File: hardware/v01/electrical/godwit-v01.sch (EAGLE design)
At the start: 23 parts, among them J1 USB-MINIB-M26FTR, U1 BQ24251, U2 LM3668-3034

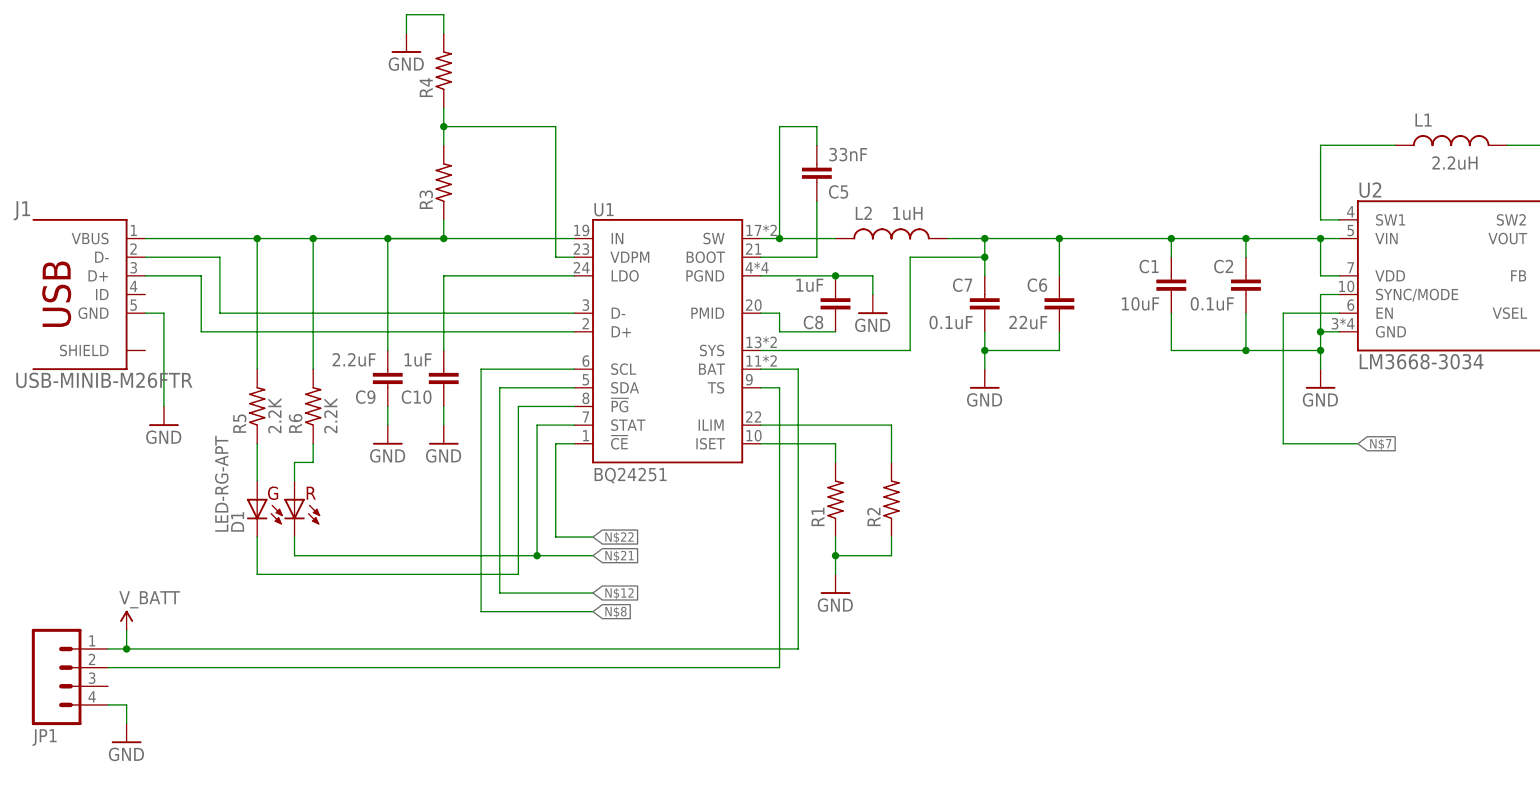
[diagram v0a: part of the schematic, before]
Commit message: rearranged and added circuits
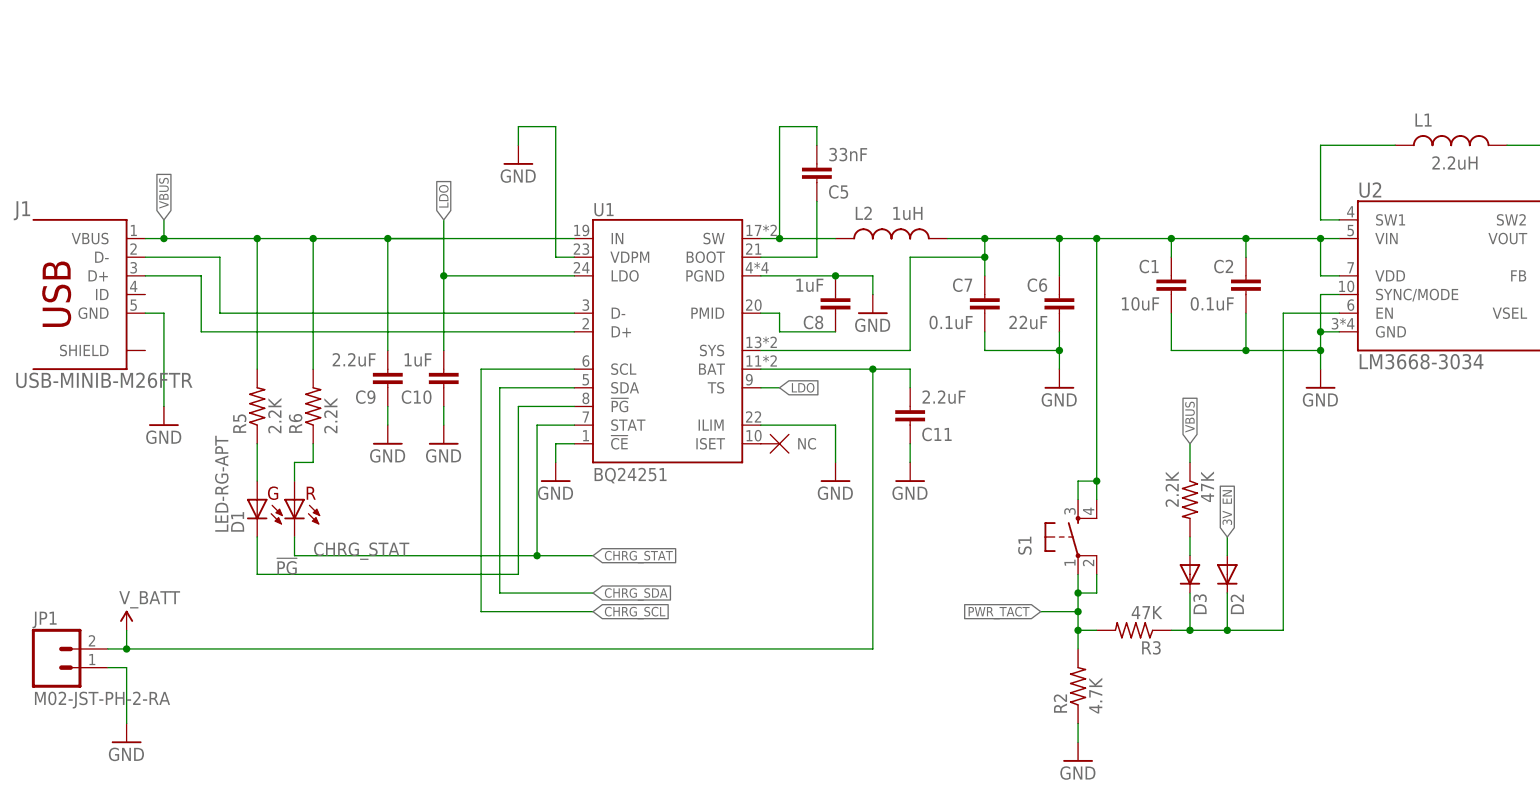
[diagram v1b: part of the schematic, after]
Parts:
- removed R1, R4: (no value), hybridpi-rcl:R-US_R0603
- added 47K: 2.2K, hybridpi-rcl:R-US_R0603
- added C11: 2.2uF, hybridpi-rcl:C-EUC0603
- added D2, D3: (no value), hybridpi-discrete-semi:DIODESOD523
- added S1: (no value), hybridpi-electromechanical:TAC_SWITCHPTH
- added U$1: NC, hybridpi-aesthetics:NC
- C10, C8: VOLTAGE (none) -> >=10V
- C5: VOLTAGE (none) -> >15
- JP1: value (none) -> M02-JST-PH-2-RA; device hybridpi-connector:M04-JST-PH-4-RA -> hybridpi-connector:M02-JST-PH-2-RA
- R2: value (none) -> 4.7K
- R3: value (none) -> 47K
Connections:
- net N$12 renamed CHRG_SDA
- net N$20 renamed !PG!
- net N$21 renamed CHRG_STAT
- net N$8 renamed CHRG_SCL
- removed net N$10: R2.2, U1.ILIM
- removed net N$11: R3.2, R4.1, U1.VDPM
- removed net N$13: JP1.2, U1.TS
- removed net N$14: C10.2, U1.LDO
- removed net N$19: C9.2, J1.VBUS, R3.1, R5.2, R6.2, U1.IN
- removed net N$22: U1.!CE!
- new net 3V_EN: D2.A
- new net LDO: C10.2, U1.LDO, U1.TS
- new net N$8: 47K.2, D3.A
- new net PWR_TACT: R2.2, R3.2, S1.1, S1.2
- new net VBUS: 47K.1, C9.2, J1.VBUS, R5.2, R6.2, U1.IN
- net GND: now also C11.1, JP1.1, U1.!CE!, U1.ILIM, U1.VDPM; no longer JP1.4, R1.1, R4.2
- net N$4: now also S1.3, S1.4
- net N$7: now also U$1.NC, U1.ISET; no longer U2.EN
- net N$9: now also D2.C, D3.C, R3.1, U2.EN; no longer R1.2, U1.ISET
- net V_BATT: now also C11.2, JP1.2; no longer JP1.1
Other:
- moved on the sheet: R2, R3

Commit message: Added sensing circuitry.
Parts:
- added C12, C16: 1uF, hybridpi-rcl:C-EUC0603
- added C13: 4.7uF, hybridpi-rcl:C-EUC0603
- added C14, C15, C17, C18: 0.1uF, hybridpi-rcl:C-EUC0603
- added R4, R7, R8: 220, hybridpi-rcl:R-US_R0603
- added R9: 470K, hybridpi-rcl:R-US_R0603
- added U$10, U$11, U$12, U$2, U$3, U$4, U$5, U$6, U$7, U$8, U$9: NC, hybridpi-aesthetics:NC
- added U3: UC530, hybridpi-rf:UC530
- added U4: AAT4280A, hybridpi-poweric:AAT4280A
- added U5: BMP180, hybridpi-sensor:BMP180
- added U6: MAG3110, hybridpi-sensor:MAG3110
- R1: value 2.2K -> 47K
- R2: value 4.7K -> 2.2K
- renumbered 47K to R1
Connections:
- net N$16 renamed USB_D-
- net N$17 renamed USB_D+
- new net BAR_SCL: U5.SCL
- new net BAR_SDA: U5.SDA
- new net GPS_RX: R7.2
- new net GPS_TX: R4.2
- new net MAG_SCL: U6.SCL
- new net MAG_SDA: U6.SDA
- new net N$10: U$2.NC, U3.TX1
- new net N$11: U$3.NC, U3.RX1
- new net N$12: U$4.NC, U3.PPS
- new net N$13: U$5.NC, U3.EINT1
- new net N$14: U$6.NC, U3.32K/DR_INT
- new net N$16: U$7.NC, U3.GPIO9
- new net N$17: U$8.NC, U3.GPIO10
- new net N$19: U$11.NC, U3.WAKEUP
- new net N$20: U$9.NC, U3.UI_FIX
- new net N$21: U$10.NC, U3.!RESET!
- new net N$22: C13.2, U3.VDD, U4.OUT
- new net N$23: R4.1, U3.TX0
- new net N$24: R7.1, U3.RX0
- new net N$25: R8.2, U3.TIMER
- new net N$26: R8.1, R9.1, U4.ON
- new net N$28: C18.1, U6.CAP-R
- new net N$29: C17.1, U6.CAP-A
- new net N$32: U$12.NC, U6.INT1
- new net VSYS: C1.1, C12.2, C2.1, C6.1, C7.1, L2.2, R5.2, R6.2, S1.3, S1.4, U1.SYS, U2.VDD, U2.VIN, U3.VDD_B
- net 3.0V: now also C14.1, C15.1, C16.2, R9.2, U4.IN, U5.VDD, U5.VDDIO, U6.VDD, U6.VDDIO
- net GND: now also C12.1, C13.1, C14.2, C15.2, C16.1, C17.2, C18.2, U3.GND, U4.GND, U5.GND, U6.GND
- net N$4: now also U3.ANT, U3.RF_IN; no longer C1.1, C2.1, C6.1, C7.1, L2.2, S1.3, S1.4, U1.SYS, U2.VDD, U2.VIN
- net VBUS: no longer R5.2, R6.2

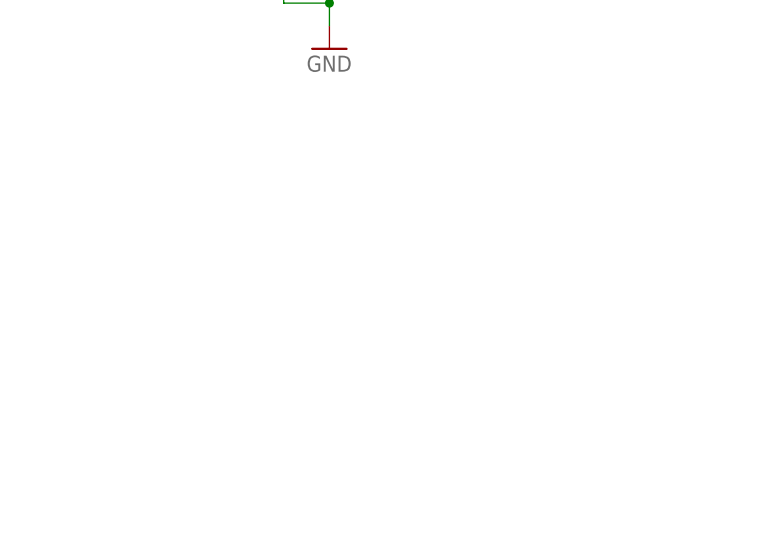
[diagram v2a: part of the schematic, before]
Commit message: Added SD card circuit.
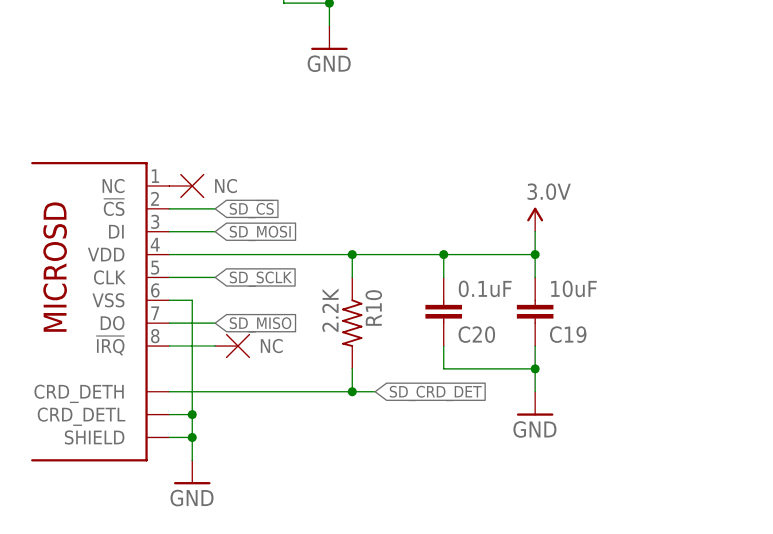
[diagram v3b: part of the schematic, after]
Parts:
- added C19: 10uF, hybridpi-rcl:C-EUC0805
- added C20: 0.1uF, hybridpi-rcl:C-EUC0603
- added JP2: MICRO-SD-5031821853, hybridpi-connector:MICRO-SD-5031821853
- added R10: 2.2K, hybridpi-rcl:R-US_R0603
- added U$13, U$14: NC, hybridpi-aesthetics:NC
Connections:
- new net N$30: JP2.NC, U$13.NC
- new net N$31: JP2.!IRQ!, U$14.NC
- new net SD_!CS!: JP2.!CS!
- new net SD_CRD_DET: JP2.CRD_DETH, R10.2
- new net SD_MISO: JP2.DO
- new net SD_MOSI: JP2.DI
- new net SD_SCLK: JP2.CLK
- net 3.0V: now also C19.2, C20.2, JP2.VDD, R10.1
- net GND: now also C19.1, C20.1, JP2.CRD_DETL, JP2.SHIELD, JP2.VSS
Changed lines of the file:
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@@
 <part name="GND19" library="SparkFun-Aesthetics" deviceset="GND" device=""/>
 <part name="SUPPLY5" library="hybridpi-aesthetics" deviceset="3.0V" device=""/>
+<part name="JP2" library="hybridpi-connector" deviceset="MICRO-SD" device="-5031821853"/>
+<part name="C19" library="hybridpi-rcl" deviceset="C-EU" device="C0805" value="10uF">
+<attribute name="VENDOR" value="DIGI-KEY"/>
+<attribute name="VENDOR_PN" value="490-6470-1-ND"/>
+</part>
+<part name="C20" library="hybridpi-rcl" deviceset="C-EU" device="C0603" value="0.1uF"/>
+<part name="R10" library="hybridpi-rcl" deviceset="R-US_" device="R0603" value="2.2K"/>
+<part name="U$13" library="hybridpi-aesthetics" deviceset="NC" device=""/>
+<part name="U$14" library="hybridpi-aesthetics" deviceset="NC" device=""/>
+<part name="GND20" library="SparkFun-Aesthetics" deviceset="GND" device=""/>
+<part name="GND21" library="SparkFun-Aesthetics" deviceset="GND" device=""/>
+<part name="SUPPLY6" library="hybridpi-aesthetics" deviceset="3.0V" device=""/>
 </parts>
 <sheets>
@@
 <instance part="GND19" gate="1" x="154.94" y="104.14"/>
 <instance part="SUPPLY5" gate="G$1" x="154.94" y="132.08"/>
+<instance part="JP2" gate="G$1" x="17.78" y="86.36"/>
+<instance part="C19" gate="G$1" x="66.04" y="83.82" rot="MR180">
+<attribute name="VENDOR" x="66.04" y="83.82" size="1.778" layer="96" rot="MR180" display="off"/>
+<attribute name="VENDOR_PN" x="66.04" y="83.82" size="1.778" layer="96" rot="MR180" display="off"/>
+</instance>
+<instance part="C20" gate="G$1" x="55.88" y="83.82" rot="MR180"/>
+<instance part="R10" gate="G$1" x="45.72" y="83.82" rot="R270"/>
+<instance part="U$13" gate="G$1" x="25.4" y="99.06"/>
+<instance part="U$14" gate="G$1" x="30.48" y="81.28"/>
+<instance part="GND20" gate="1" x="27.94" y="66.04"/>
+<instance part="GND21" gate="1" x="66.04" y="73.66"/>
+<instance part="SUPPLY6" gate="G$1" x="66.04" y="93.98"/>
 </instances>
 <busses>
@@
 <wire x1="154.94" y1="109.22" x2="154.94" y2="106.68" width="0.1524" layer="91"/>
 <junction x="154.94" y="109.22"/>
+</segment>
+<segment>
+<pinref part="JP2" gate="G$1" pin="CRD_DETL"/>
+<wire x1="25.4" y1="73.66" x2="27.94" y2="73.66" width="0.1524" layer="91"/>
+<wire x1="27.94" y1="73.66" x2="27.94" y2="71.12" width="0.1524" layer="91"/>
+<pinref part="JP2" gate="G$1" pin="SHIELD"/>
+<wire x1="27.94" y1="71.12" x2="27.94" y2="68.58" width="0.1524" layer="91"/>
+<wire x1="25.4" y1="71.12" x2="27.94" y2="71.12" width="0.1524" layer="91"/>
+<junction x="27.94" y="71.12"/>
+<pinref part="JP2" gate="G$1" pin="VSS"/>
+<wire x1="25.4" y1="86.36" x2="27.94" y2="86.36" width="0.1524" layer="91"/>
+<wire x1="27.94" y1="86.36" x2="27.94" y2="73.66" width="0.1524" layer="91"/>
+<junction x="27.94" y="73.66"/>
+<pinref part="GND20" gate="1" pin="GND"/>
+</segment>
+<segment>
+<pinref part="C19" gate="G$1" pin="1"/>
+<wire x1="66.04" y1="81.28" x2="66.04" y2="78.74" width="0.1524" layer="91"/>
+<pinref part="C20" gate="G$1" pin="1"/>
+<wire x1="66.04" y1="78.74" x2="55.88" y2="78.74" width="0.1524" layer="91"/>
+<wire x1="55.88" y1="78.74" x2="55.88" y2="81.28" width="0.1524" layer="91"/>
+<pinref part="GND21" gate="1" pin="GND"/>
+<wire x1="66.04" y1="78.74" x2="66.04" y2="76.2" width="0.1524" layer="91"/>
+<junction x="66.04" y="78.74"/>
 </segment>
 </net>
@@
 <junction x="154.94" y="129.54"/>
 </segment>
+<segment>
+<pinref part="JP2" gate="G$1" pin="VDD"/>
+<pinref part="R10" gate="G$1" pin="1"/>
+<wire x1="25.4" y1="91.44" x2="45.72" y2="91.44" width="0.1524" layer="91"/>
+<wire x1="45.72" y1="91.44" x2="45.72" y2="88.9" width="0.1524" layer="91"/>
+<pinref part="C20" gate="G$1" pin="2"/>
+<wire x1="45.72" y1="91.44" x2="55.88" y2="91.44" width="0.1524" layer="91"/>
+<wire x1="55.88" y1="91.44" x2="55.88" y2="88.9" width="0.1524" layer="91"/>
+<junction x="45.72" y="91.44"/>
+<pinref part="C19" gate="G$1" pin="2"/>
+<wire x1="55.88" y1="91.44" x2="66.04" y2="91.44" width="0.1524" layer="91"/>
+<wire x1="66.04" y1="91.44" x2="66.04" y2="88.9" width="0.1524" layer="91"/>
+<junction x="55.88" y="91.44"/>
+<pinref part="SUPPLY6" gate="G$1" pin="3.0V"/>
+<wire x1="66.04" y1="93.98" x2="66.04" y2="91.44" width="0.1524" layer="91"/>
+<junction x="66.04" y="91.44"/>
+</segment>
 </net>
 <net name="N$3" class="0">
@@
 </segment>
 </net>
+<net name="N$30" class="0">
+<segment>
+<pinref part="JP2" gate="G$1" pin="NC"/>
+<pinref part="U$13" gate="G$1" pin="NC"/>
+</segment>
+</net>
+<net name="N$31" class="0">
+<segment>
+<pinref part="JP2" gate="G$1" pin="!IRQ!"/>
+<pinref part="U$14" gate="G$1" pin="NC"/>
+<wire x1="30.48" y1="81.28" x2="25.4" y2="81.28" width="0.1524" layer="91"/>
+</segment>
+</net>
+<net name="SD_!CS!" class="0">
+<segment>
+<pinref part="JP2" gate="G$1" pin="!CS!"/>
+<wire x1="25.4" y1="96.52" x2="30.48" y2="96.52" width="0.1524" layer="91"/>
+<label x="30.48" y="96.52" size="1.27" layer="95" xref="yes"/>
+</segment>
+</net>
+<net name="SD_MOSI" class="0">
+<segment>
+<pinref part="JP2" gate="G$1" pin="DI"/>
+<wire x1="25.4" y1="93.98" x2="30.48" y2="93.98" width="0.1524" layer="91"/>
+<label x="30.48" y="93.98" size="1.27" layer="95" xref="yes"/>
+</segment>
+</net>
+<net name="SD_SCLK" class="0">
+<segment>
+<pinref part="JP2" gate="G$1" pin="CLK"/>
+<wire x1="25.4" y1="88.9" x2="30.48" y2="88.9" width="0.1524" layer="91"/>
+<label x="30.48" y="88.9" size="1.27" layer="95" xref="yes"/>
+</segment>
+</net>
+<net name="SD_MISO" class="0">
+<segment>
+<pinref part="JP2" gate="G$1" pin="DO"/>
+<wire x1="25.4" y1="83.82" x2="30.48" y2="83.82" width="0.1524" layer="91"/>
+<label x="30.48" y="83.82" size="1.27" layer="95" xref="yes"/>
+</segment>
+</net>
+<net name="SD_CRD_DET" class="0">
+<segment>
+<pinref part="JP2" gate="G$1" pin="CRD_DETH"/>
+<pinref part="R10" gate="G$1" pin="2"/>
+<wire x1="25.4" y1="76.2" x2="45.72" y2="76.2" width="0.1524" layer="91"/>
+<wire x1="45.72" y1="76.2" x2="45.72" y2="78.74" width="0.1524" layer="91"/>
+<wire x1="45.72" y1="76.2" x2="48.26" y2="76.2" width="0.1524" layer="91"/>
+<junction x="45.72" y="76.2"/>
+<label x="48.26" y="76.2" size="1.27" layer="95" xref="yes"/>
+</segment>
+</net>

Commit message: Added LCD and uC to circuit
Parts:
- added C21, C22, C24, C25, C26, C27, C28, C29, C30, C31, C32, C33: 1uF, hybridpi-rcl:C-EUC0603
- added C23: DNP, hybridpi-rcl:C-EUC0603
- added R11: 0R, hybridpi-rcl:R-US_R0603
- added U$15: 128240D, hybridpi-connector:128240D
- added U$16, U$17: NC, hybridpi-aesthetics:NC
- added U7: ATUCL4U-TQFP48, hybridpi-digitalic:ATUCL4U-TQFP48
- R10: value 2.2K -> 47K
- R4, R7, R8: value 220 -> 220R
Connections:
- new net LCD_!CS!: U$15.XCS
- new net LCD_!RST!: U$15.RST
- new net LCD_A0: U$15.A0
- new net LCD_D0: U$15.D0
- new net LCD_D1: U$15.D1
- new net LCD_D2: U$15.D2
- new net LCD_D3: U$15.D3
- new net LCD_D4: U$15.D4
- new net LCD_D5: U$15.D5
- new net LCD_D6: U$15.D6
- new net LCD_D7: U$15.D7
- new net LCD_RD: U$15.E_RD
- new net LCD_WR: U$15.RW/WR
- new net N$27: C21.2, C22.1, C23.1, U$15.C2N
- new net N$33: C21.1, U$15.C2P
- new net N$34: C22.2, U$15.C4P
- new net N$35: C23.2, R11.1, U$15.C6P
- new net N$36: C24.2, C25.1, C26.1, U$15.C1N
- new net N$37: C24.1, U$15.C1P
- new net N$38: C25.2, U$15.C3P
- new net N$39: C26.2, U$15.C5P
- new net N$40: C28.1, U$15.V4
- new net N$41: C29.1, U$15.V3
- new net N$42: C27.1, R11.2, U$15.C7P, U$15.VLCD
- new net N$43: C30.1, U$15.V2
- new net N$44: C31.1, U$15.V1
- new net N$45: C32.1, U$15.V0IN, U$15.V0OUT
- new net N$51: U$15.SCL, U$16.NC
- new net N$52: U$15.SI, U$17.NC
- net 3.0V: now also C33.2, U$15.IF1, U$15.IF2, U$15.VDD
- net GND: now also C27.2, C28.2, C29.2, C30.2, C31.2, C32.2, C33.1, U$15.IF3, U$15.SHIELD, U$15.VSS
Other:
- moved on the sheet: C1, C10, C11, C14, C15, C16, C17, C18, C19, C2, C20, C3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

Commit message: Added LCD signals and EXTINT.
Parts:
- added R12, R13, R14, R15: 100K, hybridpi-rcl:R-US_R0603
- added S2, S3, S4, S5: (no value), hybridpi-electromechanical:TAC_SWITCHPTH
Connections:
- removed net BAR_SCL: U5.SCL
- removed net BAR_SDA: U5.SDA
- removed net MAG_SCL: U6.SCL
- removed net MAG_SDA: U6.SDA
- new net B_BCK: R15.1, S5.3, S5.4, U7.PB09
- new net B_DWN: R14.1, S4.3, S4.4, U7.PB08
- new net B_SEL: R13.1, S3.3, S3.4, U7.PA15
- new net B_UP: R12.1, S2.3, S2.4, U7.PA16
- new net SENS_SCL: U5.SCL, U6.SCL, U7.PB05
- new net SENS_SDA: U5.SDA, U6.SDA, U7.PA21
- net 3.0V: now also R12.2, R13.2, R14.2, R15.2
- net CHRG_SCL: now also U7.PA04
- net CHRG_SDA: now also U7.PA17
- net CHRG_STAT: now also U7.PA13
- net GND: now also S2.1, S2.2, S3.1, S3.2, S4.1, S4.2, S5.1, S5.2
- net GPS_RX: now also U7.PB06
- net GPS_TX: now also U7.PB07
- net LCD_!CS!: now also U7.PA01
- net LCD_!RST!: now also U7.PA02
- net LCD_A0: now also U7.PA18
- net LCD_D0: now also U7.PA10
- net LCD_D1: now also U7.PA12
- net LCD_D2: now also U7.PA09
- net LCD_D3: now also U7.PA08
- net LCD_D4: now also U7.PA03
- net LCD_D5: now also U7.PB12
- net LCD_D6: now also U7.PA22
- net LCD_D7: now also U7.PA00
- net LCD_RD: now also U7.PA05
- net LCD_WR: now also U7.PB11
- net PWR_TACT: now also U7.PB10
- net SD_!CS!: now also U7.PB00
- net SD_MISO: now also U7.PB02
- net SD_MOSI: now also U7.PB03
- net SD_SCLK: now also U7.PA06
- net USB_D+: now also U7.PB14
- net USB_D-: now also U7.PB13
